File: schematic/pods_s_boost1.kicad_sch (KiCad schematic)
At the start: 3 parts

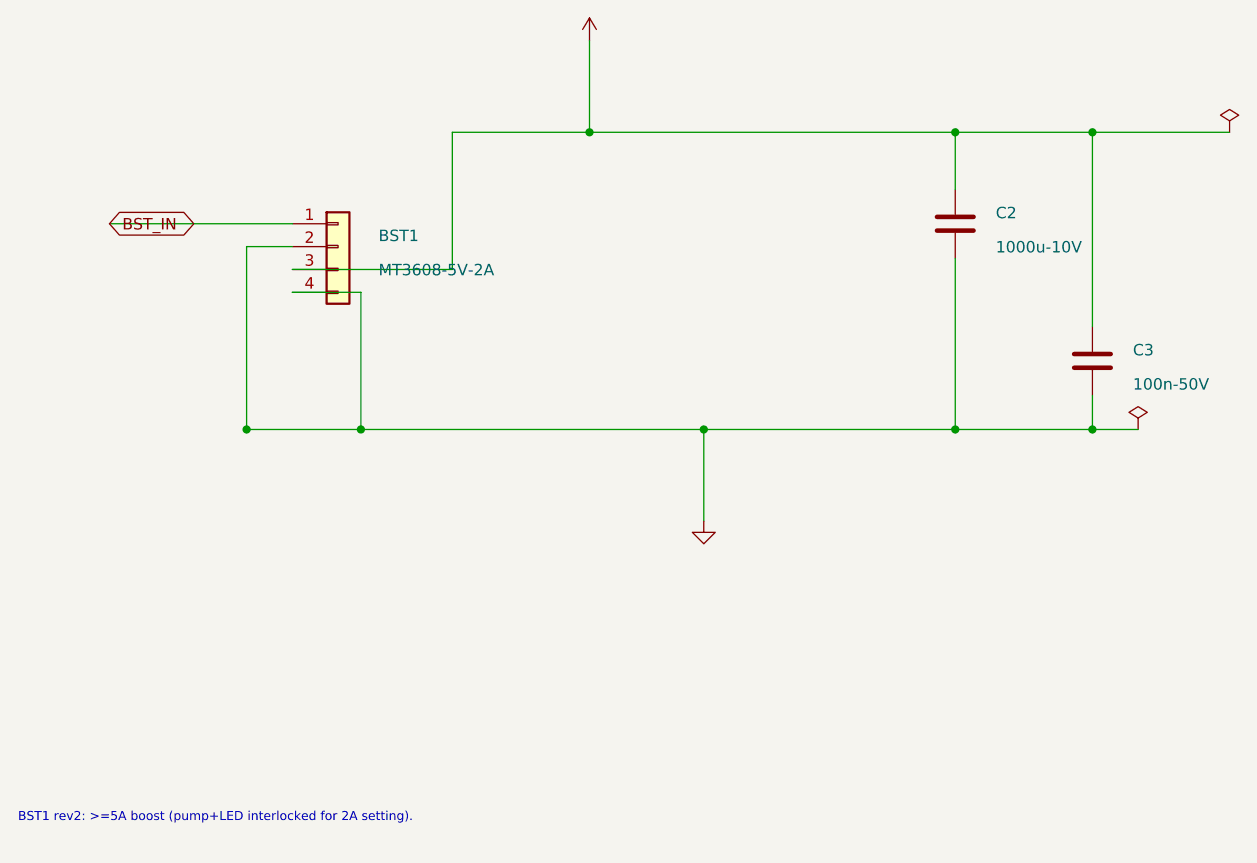
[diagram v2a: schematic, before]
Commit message: Owner decisions: OUT+/- rewire (CELL_NEG), XL6009 boost, server XOR
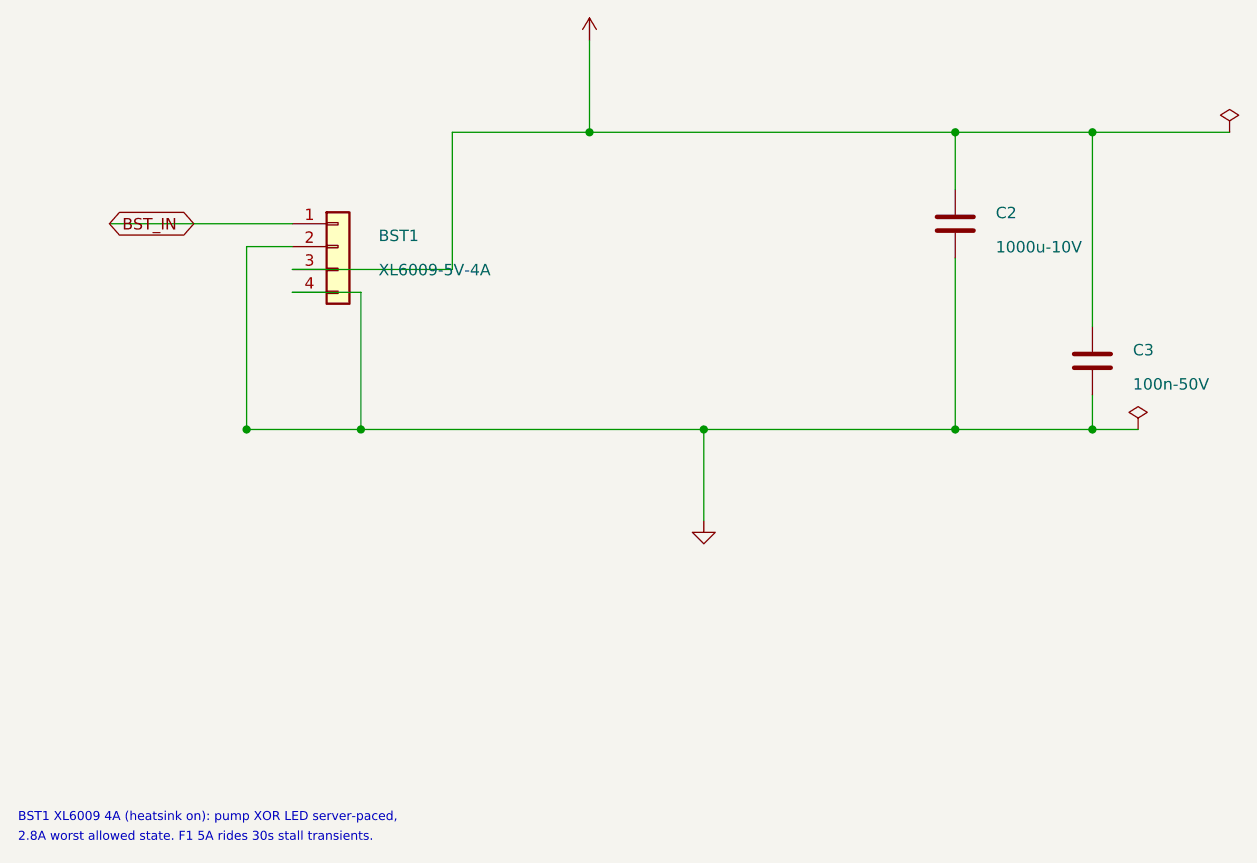
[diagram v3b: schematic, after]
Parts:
- BST1: value MT3608-5V-2A -> XL6009-5V-4A
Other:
- note added: "2.8A worst allowed state. F1 5A rides 30s stall transients."
- note added: "BST1 XL6009 4A (heatsink on): pump XOR LED server-paced,"
- note removed: "BST1 rev2: >=5A boost (pump+LED interlocked for 2A setting)."
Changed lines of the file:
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@@
       (at 65.46 75.0 0)
       (effects (font (size 1.27 1.27)) (justify left)))
-    (property "Value" "MT3608-5V-2A"
+    (property "Value" "XL6009-5V-4A"
       (at 65.46 78.8 0)
       (effects (font (size 1.27 1.27)) (justify left)))
@@
     (stroke (width 0.1524) (type default))
 )
-  (text "BST1 rev2: >=5A boost (pump+LED interlocked for 2A setting)."
+  (text "BST1 XL6009 4A (heatsink on): pump XOR LED server-paced,"
     (at 25.4 139.7 0)
     (effects (font (size 1.0 1.0)) (justify left))
 )
+  (text "2.8A worst allowed state. F1 5A rides 30s stall transients."
+    (at 25.4 141.9 0)
+    (effects (font (size 1.0 1.0)) (justify left))
+)
